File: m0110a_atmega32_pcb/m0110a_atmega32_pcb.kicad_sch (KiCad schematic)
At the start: 9 parts, among them J1 Conn_01x40_Pin, J2 ISP, J3 Serial, U2 ATmega32A-M, Y1 8 MHz

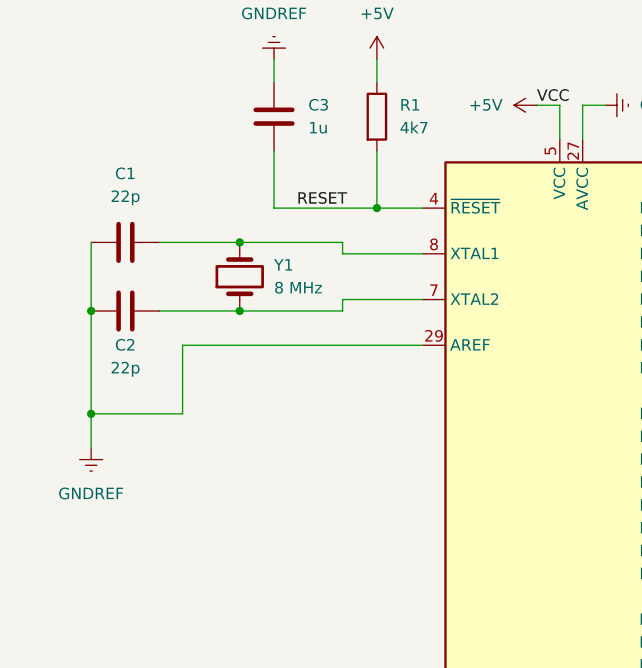
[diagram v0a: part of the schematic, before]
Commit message: Updated PCB to use more readily available parts
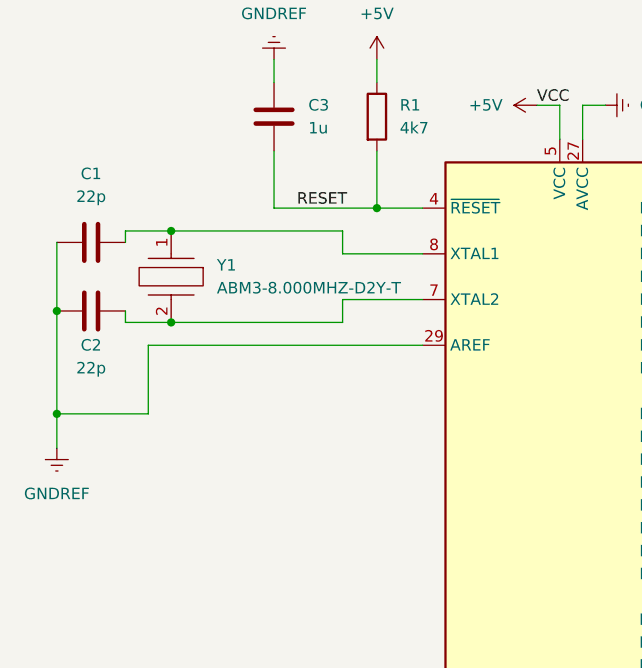
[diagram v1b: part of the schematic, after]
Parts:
- removed Y1: 8 MHz, Crystal:Crystal_SMD_2012-2Pin_2.0x1.2mm, symbol Device:Crystal
- added Y1: ABM3-8.000MHZ-D2Y-T, ABM3, symbol m0110a:ABM3-8.000MHZ-D2Y-T
- J1: footprint m0110a:Conn_2.54_W15.24mm -> m0110a:Header_2.54_W15.24mm
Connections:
- net at C1.2, U2.8 (XTAL1): now also Y1.1
- net at C2.2, U2.7 (XTAL2): now also Y1.2
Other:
- moved on the sheet: C1, C2

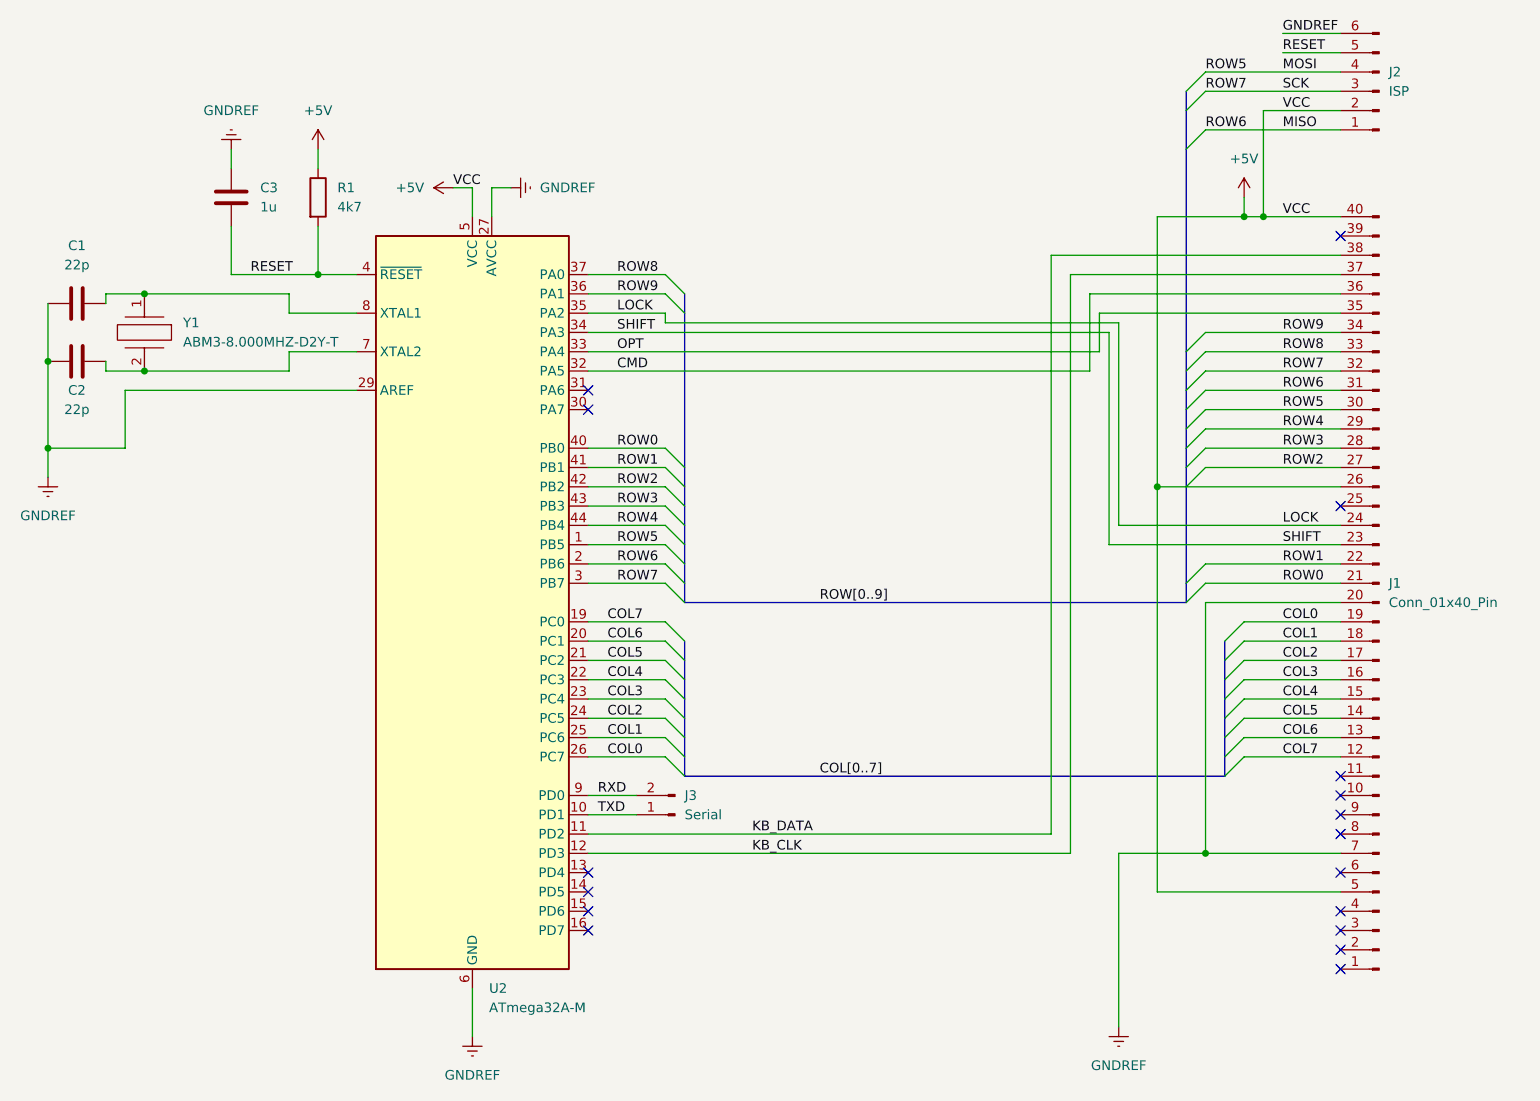
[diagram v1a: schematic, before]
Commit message: Switched from external to internal clocking
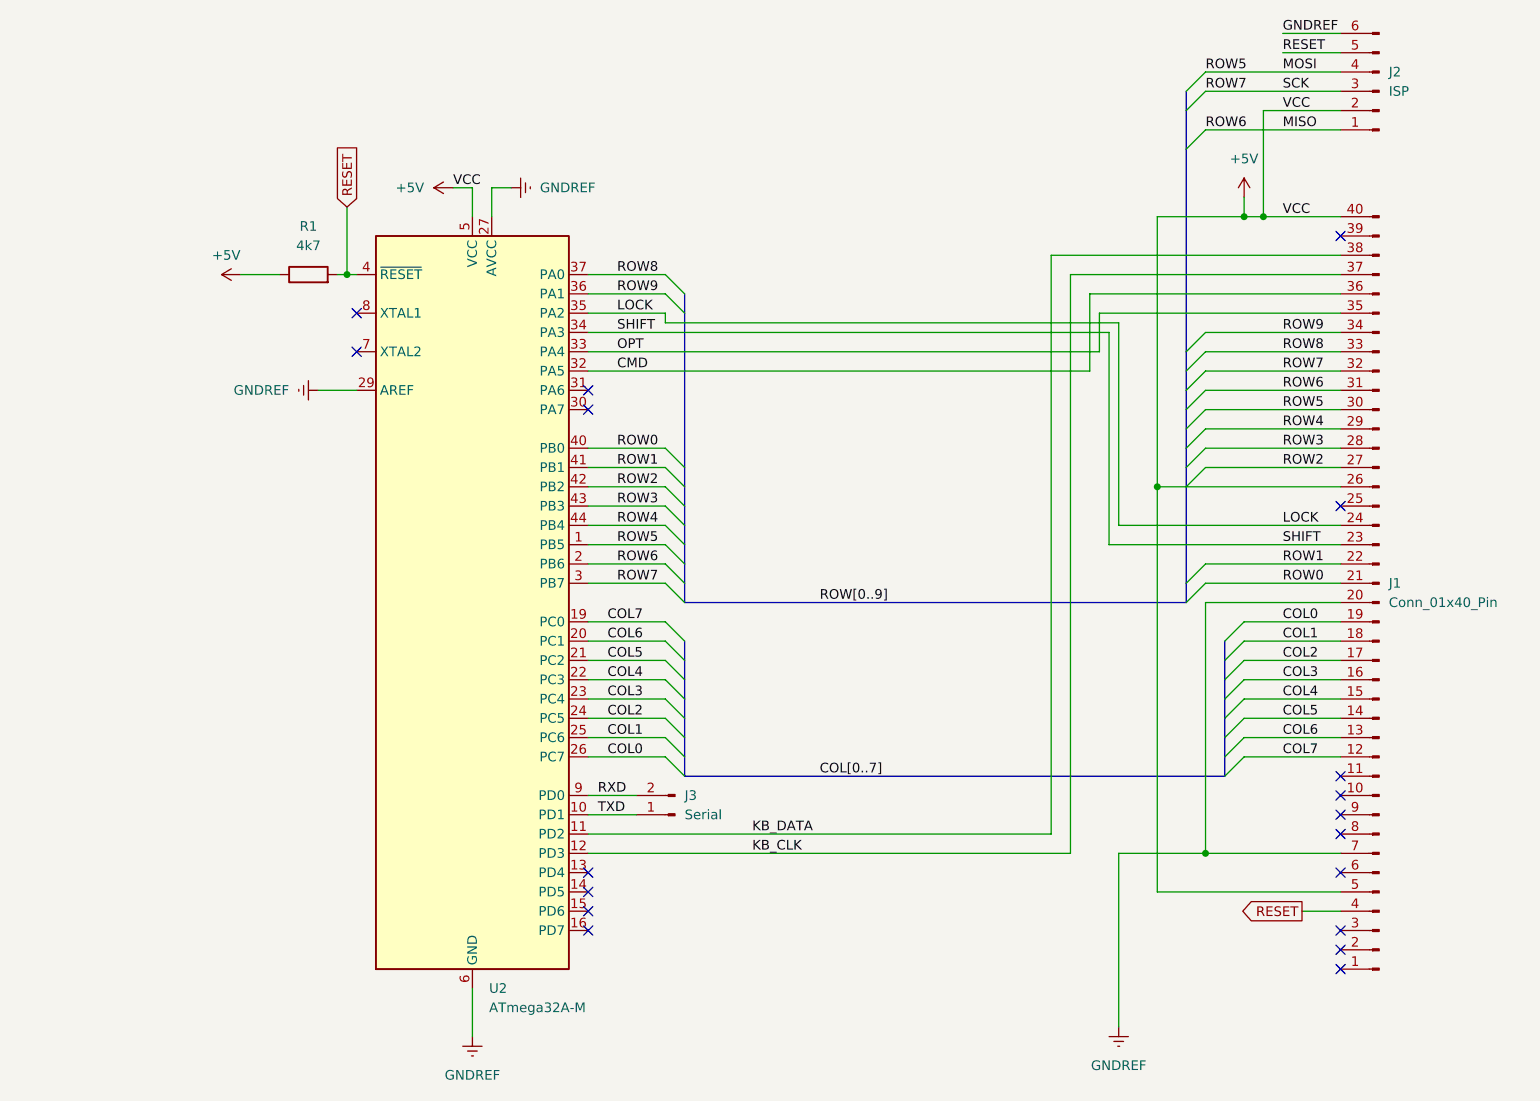
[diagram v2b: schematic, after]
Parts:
- removed C1, C2: 22p, Capacitor_SMD:C_0805_2012Metric, symbol Device:C
- removed C3: 1u, Capacitor_SMD:C_0805_2012Metric, symbol Device:C
- removed Y1: ABM3-8.000MHZ-D2Y-T, ABM3, symbol m0110a:ABM3-8.000MHZ-D2Y-T
- R1: footprint Resistor_SMD:R_0805_2012Metric -> Resistor_SMD:R_0805_2012Metric_Pad1.20x1.40mm_HandSolder
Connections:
- net RESET: now also J1.4 (Pin_4)
- no-connect marks 17 -> 18
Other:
- moved on the sheet: R1

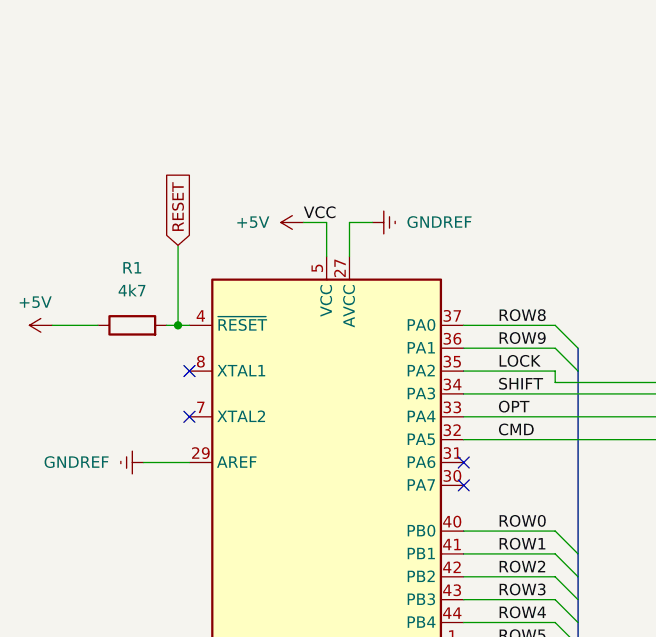
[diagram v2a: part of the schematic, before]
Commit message: Removed unneeded resistor and ground connections
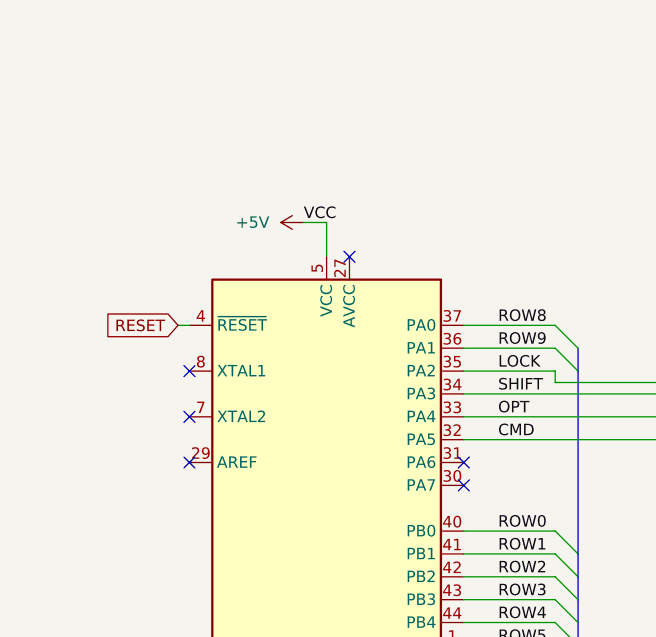
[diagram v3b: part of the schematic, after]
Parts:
- removed R1: 4k7, Resistor_SMD:R_0805_2012Metric_Pad1.20x1.40mm_HandSolder, symbol Device:R
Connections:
- net GNDREF: no longer U2.27 (AVCC), U2.29 (AREF)
- no-connect marks 18 -> 20
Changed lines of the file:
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@@
   (junction (at 193.04 81.28) (diameter 0) (color 0 0 0 0)
-  )
-  (junction (at 86.36 53.34) (diameter 0) (color 0 0 0 0)
   )
   (junction (at 199.39 129.54) (diameter 0) (color 0 0 0 0)
@@
   (no_connect (at 118.11 71.12))
   (no_connect (at 217.17 119.38))
+  (no_connect (at 87.63 68.58))
   (no_connect (at 217.17 139.7))
+  (no_connect (at 105.41 45.72))
   (no_connect (at 118.11 134.62))
   (no_connect (at 217.17 48.26))
@@
     (stroke (width 0) (type default))
   )
-  (wire (pts (xy 86.36 53.34) (xy 85.09 53.34))
-    (stroke (width 0) (type default))
-  )
   (bus (pts (xy 201.93 106.68) (xy 201.93 109.22))
     (stroke (width 0) (type default))
@@
     (stroke (width 0) (type default))
   )
-  (wire (pts (xy 105.41 41.91) (xy 105.41 45.72))
-    (stroke (width 0) (type default))
-  )
   (wire (pts (xy 199.39 68.58) (xy 217.17 68.58))
     (stroke (width 0) (type default))
@@
     (stroke (width 0) (type default))
   )
-  (wire (pts (xy 87.63 53.34) (xy 86.36 53.34))
+  (wire (pts (xy 86.36 53.34) (xy 87.63 53.34))
     (stroke (width 0) (type default))
   )
@@
     (stroke (width 0) (type default))
   )
-  (wire (pts (xy 82.55 68.58) (xy 87.63 68.58))
-    (stroke (width 0) (type default))
-  )
   (bus (pts (xy 130.81 111.76) (xy 130.81 114.3))
     (stroke (width 0) (type default))
@@
     (stroke (width 0) (type default))
   )
-  (wire (pts (xy 86.36 44.45) (xy 86.36 53.34))
-    (stroke (width 0) (type default))
-  )
   (bus (pts (xy 130.81 81.28) (xy 130.81 83.82))
     (stroke (width 0) (type default))
@@
     (stroke (width 0) (type default))
   )
-  (wire (pts (xy 72.39 53.34) (xy 77.47 53.34))
-    (stroke (width 0) (type default))
-  )
   (bus (pts (xy 130.81 93.98) (xy 130.81 96.52))
     (stroke (width 0) (type default))
@@
     (stroke (width 0) (type default))
   )
-  (wire (pts (xy 107.95 41.91) (xy 105.41 41.91))
-    (stroke (width 0) (type default))
-  )
   (wire (pts (xy 204.47 114.3) (xy 217.17 114.3))
     (stroke (width 0) (type default))
@@
     (effects (font (size 1.27 1.27)) (justify left bottom))
   )
-  (global_label "RESET" (shape input) (at 86.36 44.45 90) (fields_autoplaced)
-    (effects (font (size 1.27 1.27)) (justify left))
-    (property "Intersheetrefs" "${INTERSHEET_REFS}" (at 86.36 35.7197 90)
-      (effects (font (size 1.27 1.27)) (justify left) hide)
+  (global_label "RESET" (shape input) (at 86.36 53.34 180) (fields_autoplaced)
+    (effects (font (size 1.27 1.27)) (justify right))
+    (property "Intersheetrefs" "${INTERSHEET_REFS}" (at 77.6297 53.34 0)
+      (effects (font (size 1.27 1.27)) (justify right) hide)
     )
   )
@@
     )
   )
-  (symbol (lib_id "power:+5V") (at 72.39 53.34 90) (unit 1)
-    (in_bom yes) (on_board yes) (dnp no)
-    (property "Reference" "#PWR04" (at 76.2 53.34 0)
-      (effects (font (size 1.27 1.27)) hide)
-    )
-    (property "Value" "+5V" (at 68.58 50.8 90)
-      (effects (font (size 1.27 1.27)) (justify right))
-    )
-    (property "Footprint" "" (at 72.39 53.34 0)
-      (effects (font (size 1.27 1.27)) hide)
-    )
-    (property "Datasheet" "" (at 72.39 53.34 0)
-      (effects (font (size 1.27 1.27)) hide)
-    )
-    (pin "1")
-    (instances
-      (project "m0110a_atmega32_pcb"
-        (path "/a1198300-da90-46e8-a8a2-d3cc0b3c7a24"
-          (reference "#PWR04") (unit 1)
-        )
-      )
-    )
-  )
   (symbol (lib_id "power:+5V") (at 204.47 43.18 0) (unit 1)
     (in_bom yes) (on_board yes) (dnp no) (fields_autoplaced)
@@
     )
   )
-  (symbol (lib_id "power:GNDREF") (at 107.95 41.91 90) (unit 1)
-    (in_bom yes) (on_board yes) (dnp no) (fields_autoplaced)
-    (property "Reference" "#PWR02" (at 114.3 41.91 0)
-      (effects (font (size 1.27 1.27)) hide)
-    )
-    (property "Value" "GNDREF" (at 111.76 41.91 90)
-      (effects (font (size 1.27 1.27)) (justify right))
-    )
-    (property "Footprint" "" (at 107.95 41.91 0)
-      (effects (font (size 1.27 1.27)) hide)
-    )
-    (property "Datasheet" "" (at 107.95 41.91 0)
-      (effects (font (size 1.27 1.27)) hide)
-    )
-    (pin "1")
-    (instances
-      (project "m0110a_atmega32_pcb"
-        (path "/a1198300-da90-46e8-a8a2-d3cc0b3c7a24"
-          (reference "#PWR02") (unit 1)
-        )
-      )
-    )
-  )
   (symbol (lib_id "power:GNDREF") (at 187.96 152.4 0) (unit 1)
     (in_bom yes) (on_board yes) (dnp no) (fields_autoplaced)
@@
         (path "/a1198300-da90-46e8-a8a2-d3cc0b3c7a24"
           (reference "#PWR08") (unit 1)
-        )
-      )
-    )
-  )
-  (symbol (lib_id "Device:R") (at 81.28 53.34 90) (unit 1)
-    (in_bom yes) (on_board yes) (dnp no) (fields_autoplaced)
-    (property "Reference" "R1" (at 81.28 46.99 90)
-      (effects (font (size 1.27 1.27)))
-    )
-    (property "Value" "4k7" (at 81.28 49.53 90)
-      (effects (font (size 1.27 1.27)))
-    )
-    (property "Footprint" "Resistor_SMD:R_0805_2012Metric_Pad1.20x1.40mm_HandSolder" (at 81.28 55.118 90)
-      (effects (font (size 1.27 1.27)) hide)
-    )
-    (property "Datasheet" "~" (at 81.28 53.34 0)
-      (effects (font (size 1.27 1.27)) hide)
-    )
-    (pin "1")
-    (pin "2")
-    (instances
-      (project "m0110a_atmega32_pcb"
-        (path "/a1198300-da90-46e8-a8a2-d3cc0b3c7a24"
-          (reference "R1") (unit 1)
         )
       )
@@
         )
       )
-    )
-  )
-  (symbol (lib_id "power:GNDREF") (at 82.55 68.58 270) (unit 1)
-    (in_bom yes) (on_board yes) (dnp no) (fields_autoplaced)
-    (property "Reference" "#PWR01" (at 76.2 68.58 0)
-      (effects (font (size 1.27 1.27)) hide)
-    )
-    (property "Value" "GNDREF" (at 78.74 68.58 90)
-      (effects (font (size 1.27 1.27)) (justify right))
-    )
-    (property "Footprint" "" (at 82.55 68.58 0)
-      (effects (font (size 1.27 1.27)) hide)
-    )
-    (property "Datasheet" "" (at 82.55 68.58 0)
-      (effects (font (size 1.27 1.27)) hide)
-    )
-    (pin "1")
-    (instances
-      (project "m0110a_atmega32_pcb"
-        (path "/a1198300-da90-46e8-a8a2-d3cc0b3c7a24"
-          (reference "#PWR01") (unit 1)
-        )
-      )
